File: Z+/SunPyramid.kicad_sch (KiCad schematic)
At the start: 8 parts, among them U3 SunSensor, U4 SunSensor, U5 SunSensor, U9 SunSensor

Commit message: Z+ updates WIP
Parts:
- added C5, C6, C7, C8: 100nF, Capacitor_SMD:C_0603_1608Metric, symbol Device:C_Small
- F1: footprint (none) -> Fuse:Fuse_0603_1608Metric
- F2: renamed from F5; footprint (none) -> Fuse:Fuse_0603_1608Metric
- F3: renamed from F6; footprint (none) -> Fuse:Fuse_0603_1608Metric
- F4: renamed from F7; footprint (none) -> Fuse:Fuse_0603_1608Metric
- U2: renamed from U3; footprint SolarPanels:SunSensor -> Argus-IC:SunSensor
- U3: renamed from U4; footprint SolarPanels:SunSensor -> Argus-IC:SunSensor
- U4: renamed from U5; footprint SolarPanels:SunSensor -> Argus-IC:SunSensor
- U5: renamed from U9; footprint SolarPanels:SunSensor -> Argus-IC:SunSensor
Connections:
- net GND: now also C5.2, C6.2, C7.2, C8.2
- net LS0_3V3: now also C8.1
- net LS1_3V3: now also C5.1
- net LS2_3V3: now also C6.1
- net LS3_3V3: now also C7.1

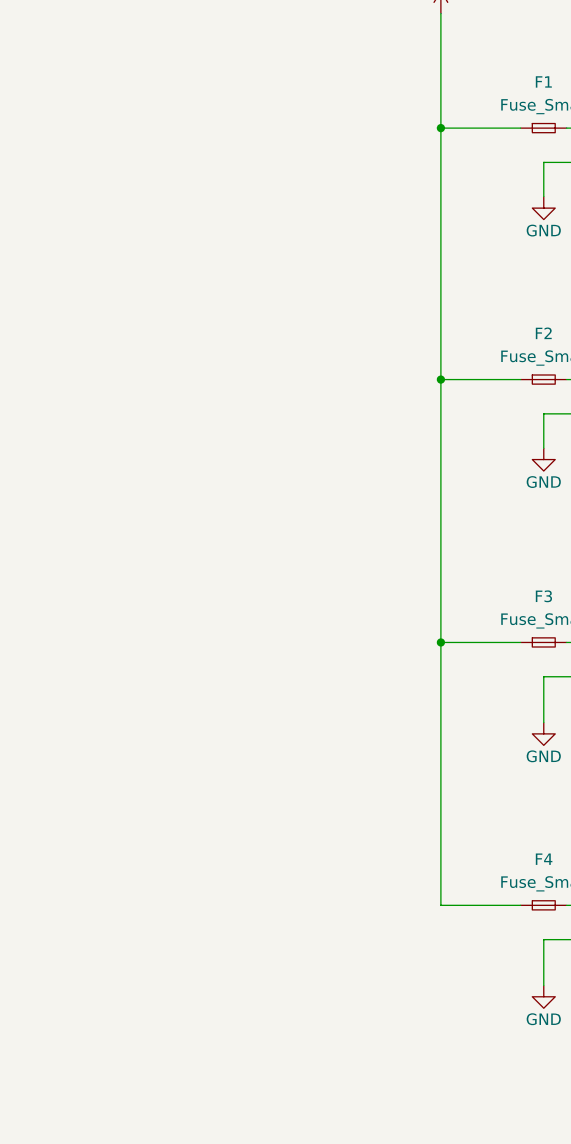
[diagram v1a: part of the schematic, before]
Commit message: Started layout of coil driver
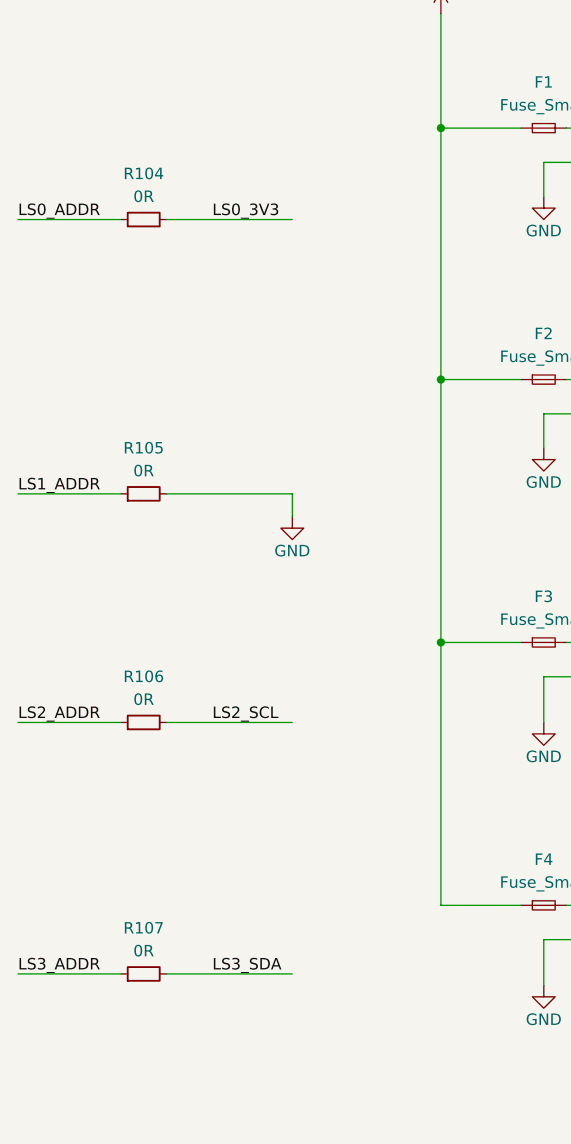
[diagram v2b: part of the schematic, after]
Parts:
- added R104, R105, R106, R107: 0R, Resistor_SMD:R_0603_1608Metric, symbol Device:R_Small
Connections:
- net GND: now also R105.2
- net LS0_3V3: now also R104.2
- net LS0_ADDR: now also R104.1
- net LS1_ADDR: now also R105.1
- net LS2_ADDR: now also R106.1
- net LS2_SCL: now also R106.2
- net LS3_ADDR: now also R107.1
- net LS3_SDA: now also R107.2
